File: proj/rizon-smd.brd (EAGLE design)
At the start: 49 parts, among them J1 PWRJACK5521, J2 DB9A-DS09AKG, P1 UART1(GND-TX-RX), P6 10k, U1 Z8400LQFP, U10 7432SOIC, U11 74138SOIC, U12 7400SOIC, U13 74590SOIC, U14 74590SOIC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

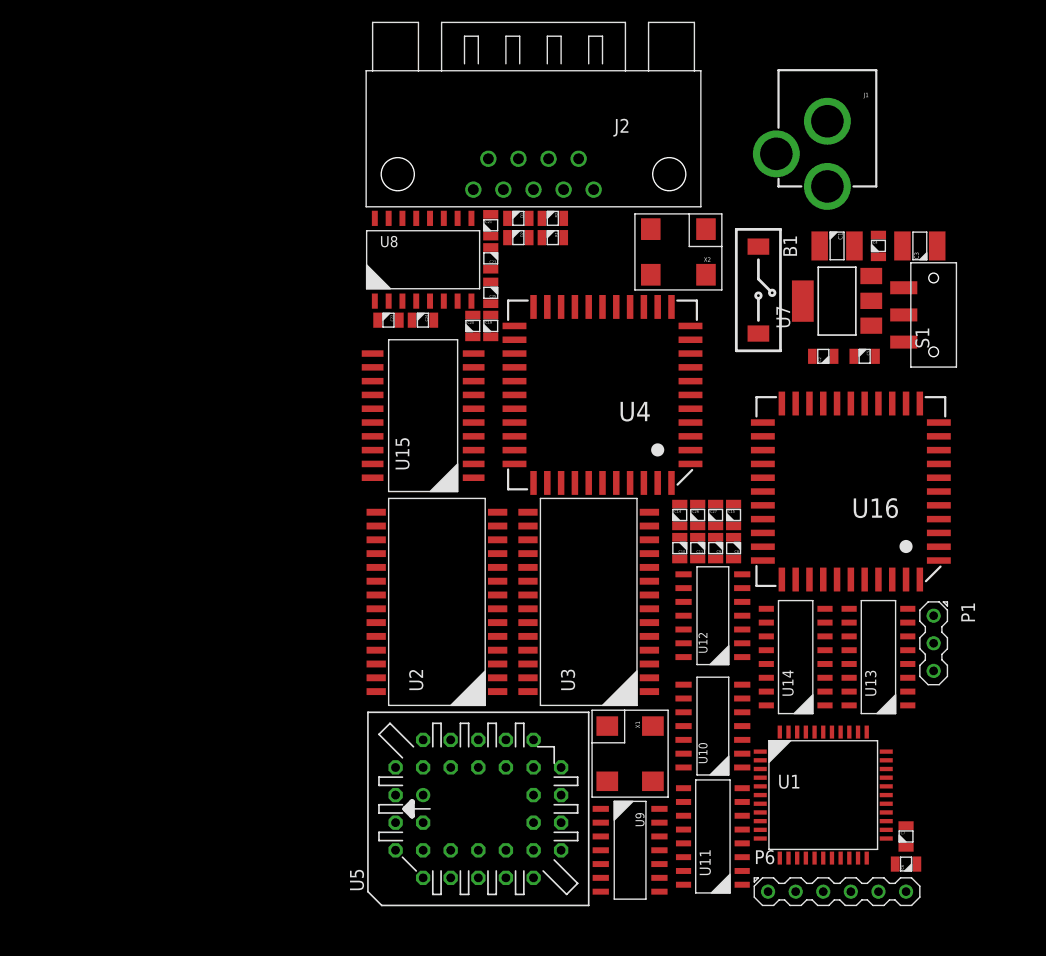
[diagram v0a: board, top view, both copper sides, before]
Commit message: Started routing SMD version of Rizon board
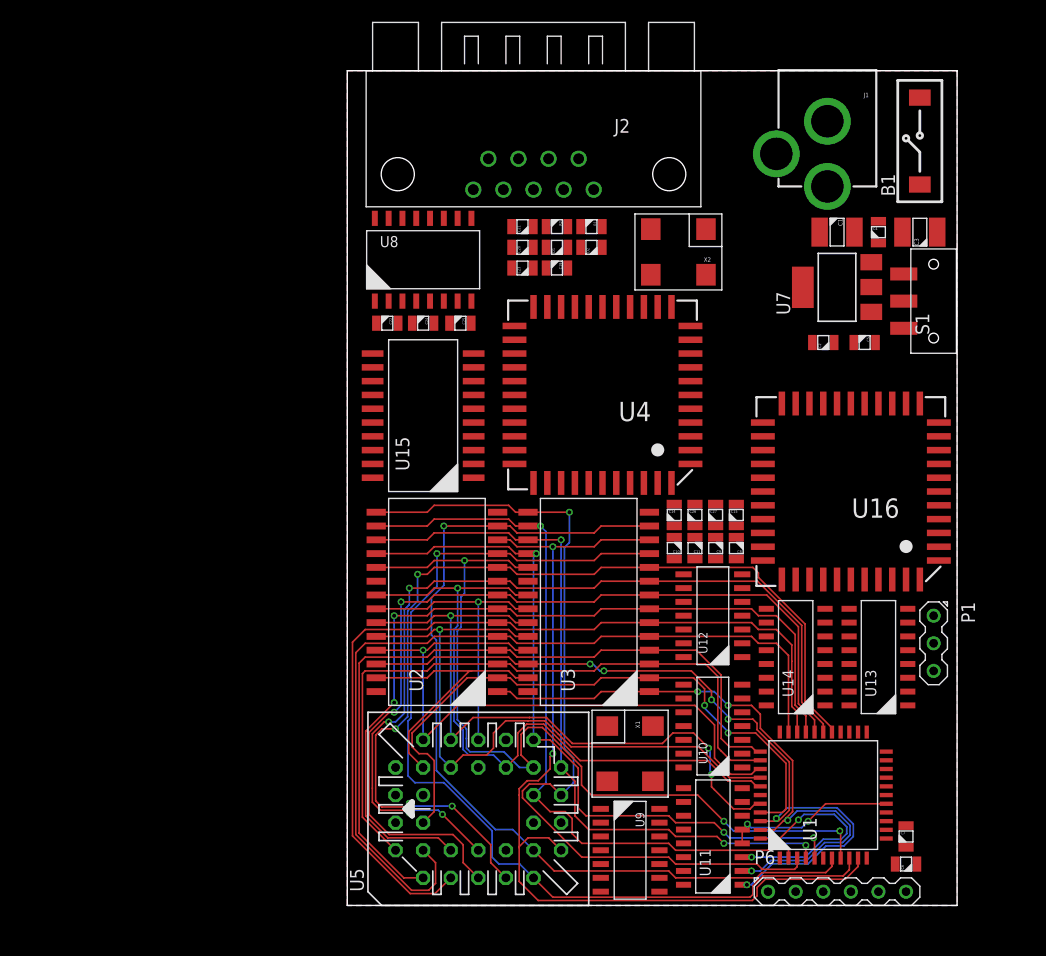
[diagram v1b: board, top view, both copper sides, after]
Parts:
- moved B1 20.2 mm to (81.3, 72.9), turned to 90 degrees
- moved C20 8.56 mm to (44.7, 63.1), turned to 0 degrees
- moved C19 8.10 mm to (47.9, 61.2), turned to 180 degrees
- moved D2 6.79 mm to (51.1, 63.1), turned to 0 degrees
- moved D1 4.44 mm to (47.9, 63.1), turned to 0 degrees
- moved C25 3.95 mm to (39.0, 56.1), turned to 180 degrees
- moved R1 3.70 mm to (51.1, 65.0)
- moved C23 3.05 mm to (44.7, 61.2), turned to 0 degrees
- moved C21 2.92 mm to (44.7, 65.0), turned to 0 degrees
- moved C1 1.27 mm to (73.7, 64.5)
- moved C2 1.27 mm to (72.4, 54.4)
- moved C3 1.27 mm to (81.3, 64.5)
- moved C4 1.27 mm to (77.5, 64.5)
- moved C5 1.27 mm to (76.2, 54.4)
- moved U7 1.27 mm to (73.7, 59.4)
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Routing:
- net DATA0: track 0.00 -> 90.9 mm, vias 0 -> 1
- net ADDR0: track 0.00 -> 89.2 mm, vias 0 -> 4
- net DATA1: track 0.00 -> 86.4 mm, vias 0 -> 2
- net DATA2: track 0.00 -> 84.3 mm, vias 0 -> 1
- net ADDR2: track 0.00 -> 83.4 mm, vias 0 -> 2
- net ADDR1: track 0.00 -> 82.8 mm, vias 0 -> 4
- net ADDR4: track 0.00 -> 80.5 mm
- net DATA7: track 0.00 -> 79.9 mm, vias 0 -> 3
- net DATA3: track 0.00 -> 79.1 mm, vias 0 -> 1
- net ADDR5: track 0.00 -> 78.7 mm
- net ADDR3: track 0.00 -> 76.7 mm, vias 0 -> 2
- net ADDR13: track 0.00 -> 72.5 mm, vias 0 -> 6
- net DATA4: track 0.00 -> 68.6 mm, vias 0 -> 1
- net ADDR6: track 0.00 -> 68.5 mm
- net DATA5: track 0.00 -> 67.0 mm, vias 0 -> 3
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- added copper zone on layer 1, net GND
- added copper zone on layer 16, net GND
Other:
- board outline added: 56.1 x 76.8 mm

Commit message: Added missing signal net (TIMER_OUT -> INT_TIMER) in Rizon I/O board Further routed SMD version of Rizon computer
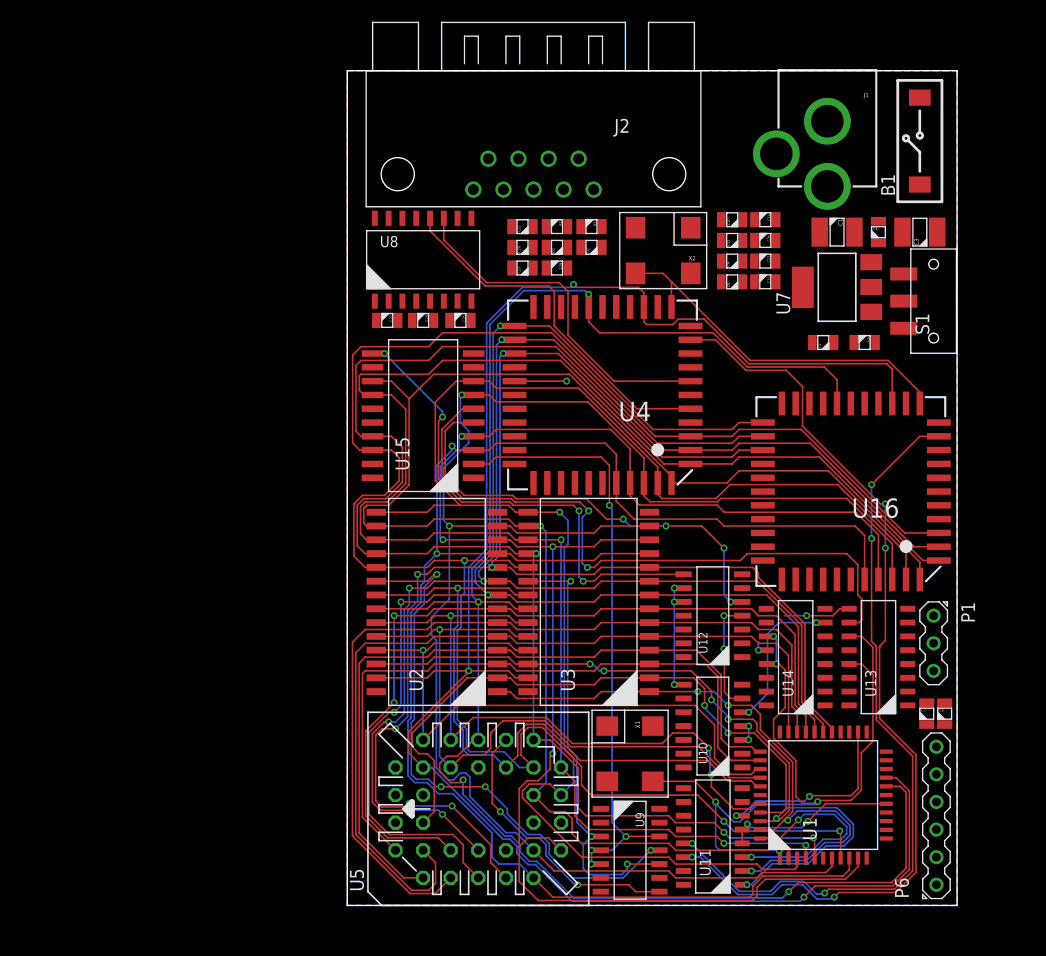
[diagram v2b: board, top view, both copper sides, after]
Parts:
- moved C10 30.7 mm to (64.0, 65.7), turned to 0 degrees
- moved C11 28.5 mm to (64.0, 63.8), turned to 0 degrees
- moved C14 28.4 mm to (67.1, 65.7), turned to 180 degrees
- moved C9 26.5 mm to (64.0, 61.8), turned to 0 degrees
- moved C26 26.1 mm to (67.1, 63.8), turned to 180 degrees
- moved C8 24.5 mm to (64.0, 59.9), turned to 0 degrees
- moved C27 23.8 mm to (67.1, 61.8), turned to 180 degrees
- moved C15 21.6 mm to (67.1, 59.9), turned to 180 degrees
- moved C6 14.3 mm to (83.6, 20.2), turned to 270 degrees
- moved P6 11.5 mm to (82.8, 10.8), turned to 90 degrees
- moved C7 11.5 mm to (81.9, 20.2)
- moved X2 1.40 mm to (57.7, 62.8)
- moved C22 0.25 mm to (32.3, 56.4)
- moved C24 0.25 mm to (35.6, 56.4)
- moved C25 0.25 mm to (39.0, 56.4)
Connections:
- removed net INT_TIMER: U10.P$5
- net TIMER_OUT: now also U10.P$5
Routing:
- net !WR: track 26.4 -> 167.4 mm, vias 0 -> 3
- net !RD: track 27.2 -> 158.5 mm, vias 1 -> 4
- net DATA7: track 79.9 -> 170.2 mm
- net DATA6: track 66.1 -> 153.6 mm
- net !IODEV1: track 0.00 -> 86.6 mm, vias 0 -> 4
- net DATA5: track 67.0 -> 151.5 mm
- net DATA4: track 68.6 -> 146.5 mm
- net CLK: track 0.00 -> 72.2 mm, vias 0 -> 5
- net !IODEV2: track 0.00 -> 69.8 mm, vias 0 -> 4
- net DATA2: track 84.3 -> 149.9 mm, vias 1 -> 2
- net DATA3: track 79.1 -> 144.6 mm
- net DATA1: track 86.4 -> 151.1 mm, vias 2 -> 4
- net !TIMER_CLR: track 0.00 -> 61.0 mm, vias 0 -> 2
- net DATA0: track 90.9 -> 149.7 mm, vias 1 -> 2
- net !ROM_EN: track 0.00 -> 57.6 mm, vias 0 -> 4
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
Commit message: Rizon SMD routing work
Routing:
- net !TIMER_CLR: track 61.0 -> 71.1 mm, vias 2 -> 4
- net N$3: track 7.69 -> 11.3 mm
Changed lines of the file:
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@@
 <wire x1="30.2768" y1="18.5928" x2="32.893" y2="21.209" width="0.1524" layer="1"/>
 <via x="32.893" y="21.209" extent="1-16" drill="0.35"/>
-<wire x1="32.893" y1="21.209" x2="32.893" y2="29.21" width="0.1524" layer="16"/>
 <via x="32.893" y="29.21" extent="1-16" drill="0.35"/>
 <wire x1="32.893" y1="29.21" x2="35.941" y2="29.21" width="0.1524" layer="1"/>
@@
 <wire x1="32.30805625" y1="8.763" x2="30.2768" y2="10.79425625" width="0.1524" layer="1"/>
 <wire x1="30.2768" y1="10.79425625" x2="30.2768" y2="18.5928" width="0.1524" layer="1"/>
+<wire x1="32.893" y1="21.209" x2="33.2232" y2="21.5392" width="0.1524" layer="16"/>
+<wire x1="33.2232" y1="28.8798" x2="32.893" y2="29.21" width="0.1524" layer="16"/>
+<wire x1="33.2232" y1="21.5392" x2="33.2232" y2="28.8798" width="0.1524" layer="16"/>
 </signal>
 <signal name="ADDR2">
@@
 <wire x1="65.405" y1="34.925" x2="74.549" y2="34.925" width="0.1524" layer="1"/>
 <wire x1="74.549" y1="34.925" x2="75.565" y2="33.909" width="0.1524" layer="1"/>
-<wire x1="75.565" y1="33.909" x2="75.565" y2="31.115" width="0.1524" layer="1"/>
+<wire x1="75.565" y1="31.115" x2="75.565" y2="33.909" width="0.1524" layer="1"/>
 <wire x1="75.565" y1="31.115" x2="75.946" y2="30.734" width="0.1524" layer="1"/>
 <wire x1="75.946" y1="30.734" x2="75.946" y2="28.829" width="0.1524" layer="1"/>
@@
 <wire x1="49.9872" y1="39.6748" x2="50.8" y2="38.862" width="0.1524" layer="1"/>
 <wire x1="43.9913125" y1="39.6748" x2="49.9872" y2="39.6748" width="0.1524" layer="1"/>
-<wire x1="64.77" y1="34.29" x2="67.15" y2="28.575" width="0" layer="19" extent="1-1"/>
+<wire x1="67.15" y1="28.575" x2="66.802" y2="28.575" width="0.1524" layer="1"/>
+<via x="66.802" y="28.575" extent="1-16" drill="0.35"/>
+<wire x1="66.802" y1="28.575" x2="67.43958125" y2="28.575" width="0.1524" layer="16"/>
+<wire x1="67.43958125" y1="28.575" x2="68.136790625" y2="29.272209375" width="0.1524" layer="16"/>
+<wire x1="68.136790625" y1="29.272209375" x2="68.70958125" y2="29.845" width="0.1524" layer="16"/>
+<wire x1="69.977" y1="29.845" x2="70.104" y2="29.972" width="0.1524" layer="16"/>
+<via x="70.104" y="29.972" extent="1-16" drill="0.35"/>
+<wire x1="70.104" y1="29.972" x2="70.612" y2="30.48" width="0.1524" layer="1"/>
+<wire x1="74.93" y1="30.48" x2="75.565" y2="31.115" width="0.1524" layer="1"/>
+<wire x1="68.70958125" y1="29.845" x2="69.977" y2="29.845" width="0.1524" layer="16"/>
+<wire x1="70.612" y1="30.48" x2="74.93" y2="30.48" width="0.1524" layer="1"/>
 </signal>
 <signal name="N$3">
@@
 <wire x1="67.15" y1="26.035" x2="66.421" y2="26.035" width="0.1524" layer="1"/>
 <via x="66.421" y="26.035" extent="1-16" drill="0.35"/>
-<wire x1="66.421" y1="26.035" x2="66.421" y2="26.797" width="0.1524" layer="16"/>
-<wire x1="68.834" y1="29.21" x2="70.866" y2="29.21" width="0.1524" layer="16"/>
 <via x="70.866" y="29.21" extent="1-16" drill="0.35"/>
 <wire x1="70.866" y1="29.21" x2="73.279" y2="29.21" width="0.1524" layer="1"/>
 <wire x1="73.279" y1="29.21" x2="73.914" y2="29.845" width="0.1524" layer="1"/>
 <wire x1="73.914" y1="29.845" x2="74.77" y2="29.845" width="0.1524" layer="1"/>
-<wire x1="66.421" y1="26.797" x2="68.834" y2="29.21" width="0" layer="19" extent="16-16"/>
+<wire x1="70.866" y1="29.21" x2="68.5056375" y2="29.21" width="0.1524" layer="16"/>
+<wire x1="68.5056375" y1="29.21" x2="66.421" y2="27.1253625" width="0.1524" layer="16"/>
+<wire x1="66.421" y1="27.1253625" x2="66.421" y2="26.035" width="0.1524" layer="16"/>
 </signal>
 <signal name="TIMER_OUT">

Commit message: Added breakouts to Rizon SMD
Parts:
- added P2: ADDR, dooba:PIN_16
- added P3: DATA, dooba:PIN_8
- added P4: CTL, dooba:PIN_16
- added P5: PWR, dooba:PIN_4
- moved C10 0.25 mm to (64.0, 65.4)
- moved C14 0.25 mm to (67.1, 65.4)
- moved C15 0.25 mm to (67.1, 59.7)
- moved C8 0.25 mm to (64.0, 59.7)
- moved C11 0.25 mm to (64.0, 63.5)
- moved C26 0.25 mm to (67.1, 63.5)
- moved C27 0.25 mm to (67.1, 61.6)
- moved C9 0.25 mm to (64.0, 61.6)
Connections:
- net !BUSACK: now also P4.7
- net !BUSREQ: now also P4.3, P6.4; no longer P6.3
- net !HALT: now also P4.10
- net !INT: now also P4.12, P6.1; no longer P6.2
- net !IORQ: now also P4.8
- net !M1: now also P4.1
- net !MREQ: now also P4.11
- net !NMI: now also P4.13, P6.2; no longer P6.1
- net !RD: now also P4.9
- net !RESET: now also P4.4, P6.5; no longer P6.4
- net !RFSH: now also P4.2
- net !ROM_EN: now also P4.14
- net !WAIT: now also P4.5, P6.3; no longer P6.5
- net !WR: now also P4.6
- net ADDR0: now also P2.1
- net ADDR1: now also P2.2
- net ADDR10: now also P2.11
- net ADDR11: now also P2.12
- net ADDR12: now also P2.13
- net ADDR13: now also P2.14
- net ADDR14: now also P2.15
- net ADDR15: now also P2.16
- net ADDR2: now also P2.3
- net ADDR3: now also P2.4
- net ADDR4: now also P2.5
- net ADDR5: now also P2.6
- net ADDR6: now also P2.7
- net ADDR7: now also P2.8
- net ADDR8: now also P2.9
- net ADDR9: now also P2.10
- net CLK: now also P4.15
- net DATA0: now also P3.1
- net DATA1: now also P3.2
- net DATA2: now also P3.3
- net DATA3: now also P3.4
- net DATA4: now also P3.5
- net DATA5: now also P3.6
- net DATA6: now also P3.7
- net DATA7: now also P3.8
- net GND: now also P4.16, P5.1, P5.3
- net VCC: now also P5.4
- net VIN: now also P5.2
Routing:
- net !RESET: track 0.00 -> 146.3 mm, vias 0 -> 9
- net VCC: track 0.00 -> 99.6 mm, vias 0 -> 2
- net !INT: track 0.00 -> 69.0 mm, vias 0 -> 5
- net RESET: track 0.00 -> 64.1 mm, vias 0 -> 5
- net INT_UART0: track 4.80 -> 52.8 mm, vias 1 -> 4
- net ADDR15: track 20.5 -> 67.0 mm, vias 2 -> 9
- net VIN: track 0.00 -> 37.8 mm, vias 0 -> 2
- net ADDR14: track 59.0 -> 89.4 mm, vias 4 -> 8
- net INT_UART1: track 0.00 -> 27.5 mm, vias 0 -> 2
- net ADDR10: track 63.1 -> 81.1 mm, vias 1 -> 3
- net !WR: track 167.4 -> 185.1 mm, vias 3 -> 5
- net ADDR11: track 61.7 -> 79.2 mm, vias 3 -> 5
- net CLK_UART0_RX: track 0.00 -> 17.3 mm, vias 0 -> 4
- net UART1_RX: track 0.00 -> 17.0 mm, vias 0 -> 2
- net !IODEV0: track 0.00 -> 16.8 mm, vias 0 -> 2
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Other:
- board size 56.1 x 76.8 mm -> 62.2 x 76.8 mm

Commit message: Rizon SMD routing
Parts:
- moved C7 1.70 mm to (83.4, 19.4), turned to 0 degrees
- moved P1 1.27 mm to (83.8, 26.7)
- moved C6 0.90 mm to (83.4, 21.1), turned to 0 degrees
- turned P5 to 270 degrees
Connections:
- net !BUSACK: now also P4.9; no longer P4.7
- net !BUSREQ: now also P4.10; no longer P4.3
- net !HALT: now also P4.5; no longer P4.10
- net !INT: now also P4.3; no longer P4.12
- net !IORQ: now also P4.7; no longer P4.8
- net !M1: now also P4.12; no longer P4.1
- net !MREQ: now also P4.6; no longer P4.11
- net !NMI: now also P4.4; no longer P4.13
- net !RD: now also P4.2; no longer P4.9
- net !RESET: now also P4.11; no longer P4.4
- net !RFSH: now also P4.13; no longer P4.2
- net !ROM_EN: now also P4.15; no longer P4.14
- net !WAIT: now also P4.8; no longer P4.5
- net !WR: now also P4.1; no longer P4.6
- net CLK: now also P4.14; no longer P4.15
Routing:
- net !ROM_EN: track 57.6 -> 104.2 mm, vias 4 -> 6
- net !RFSH: track 0.00 -> 24.1 mm, vias 0 -> 2
- net DATA0: track 149.0 -> 171.3 mm
- net !M1: track 18.0 -> 39.9 mm, vias 2 -> 4
- net DATA1: track 150.6 -> 171.4 mm, vias 4 -> 5
- net DATA2: track 149.9 -> 167.4 mm, vias 2 -> 3
- net CLK: track 72.2 -> 87.3 mm, vias 5 -> 7
- net !INT: track 69.0 -> 60.0 mm
- net UART1_RX: track 17.0 -> 8.94 mm, vias 2 -> 1
- net !IORQ: track 15.8 -> 22.3 mm, vias 2 -> 3
- net !MREQ: track 0.00 -> 6.11 mm, vias 0 -> 1
- net !HALT: track 0.00 -> 5.65 mm, vias 0 -> 1
- net UART1_TX: track 16.1 -> 11.2 mm, vias 2 -> 1
- net !RESET: track 146.3 -> 150.8 mm, vias 9 -> 10
- net !IODEV1: track 86.6 -> 87.5 mm

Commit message: Completed Rizon SMD board
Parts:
- moved B1 29.3 mm to (52.1, 70.4)
- moved J1 29.2 mm to (43.6, 73.5)
- moved P1 29.0 mm to (61.0, 44.5), flipped to the bottom
- moved C6 26.9 mm to (56.6, 23.4), turned to 90 degrees
- moved S1 26.2 mm to (59.7, 70.9)
- moved P5 25.9 mm to (61.0, 53.3), flipped to the bottom
- moved P3 25.5 mm to (1.27, 50.8), flipped to the bottom
- moved C5 25.5 mm to (50.8, 51.8)
- moved U16 25.5 mm to (49.5, 38.1)
- moved C20 25.5 mm to (19.3, 60.6)
- moved C21 25.5 mm to (19.3, 62.5)
- moved C22 25.5 mm to (6.86, 53.8)
- moved C23 25.5 mm to (19.3, 58.7)
- moved C24 25.5 mm to (10.2, 53.8)
- moved D2 25.5 mm to (25.7, 60.6)
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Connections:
- net !BUSREQ: now also P4.8; no longer P4.10
- net !HALT: now also P4.4; no longer P4.5
- net !INT: now also P4.1; no longer P4.3
- net !IORQ: now also P4.6; no longer P4.7
- net !MREQ: now also P4.5; no longer P4.6
- net !NMI: now also P4.2; no longer P4.4
- net !RD: now also P4.11; no longer P4.2
- net !RESET: now also P4.7; no longer P4.11
- net !WAIT: now also P4.3; no longer P4.8
- net !WR: now also P4.10; no longer P4.1
- net VIN: now also S1.1; no longer S1.3
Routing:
- net VCC: track 99.6 -> 436.0 mm, vias 2 -> 25
- net GND: track 0.00 -> 93.7 mm, vias 0 -> 442
- net !RD: track 158.5 -> 180.7 mm, vias 4 -> 6
- net !WR: track 185.1 -> 203.6 mm, vias 5 -> 7
- net VIN: track 37.8 -> 51.6 mm, vias 2 -> 4
- net !BUSACK: track 0.00 -> 13.7 mm, vias 0 -> 2
- net !BUSREQ: track 7.11 -> 18.6 mm, vias 1 -> 2
- net !IORQ: track 22.3 -> 28.4 mm
- net !RESET: track 150.8 -> 156.5 mm, vias 10 -> 11
- net !WAIT: track 8.74 -> 14.3 mm, vias 1 -> 2
- net !MREQ: track 6.11 -> 10.2 mm
- net UART1_TX: track 11.2 -> 7.22 mm, vias 1 -> 0
- net !INT: track 60.0 -> 63.8 mm
- net !NMI: track 5.68 -> 9.50 mm
- net !HALT: track 5.65 -> 8.65 mm
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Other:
- board text added: "!BUSACK"
- board text added: "!BUSREQ"
- board text added: "!HALT"
- board text added: "!INT"
- board text added: "!IORQ"
- board text added: "!M1"
- board text added: "!MREQ"
- board text added: "!NMI"
- board text added: "!RD"
- board text added: "!RESET"
- board text added: "!RFSH"
- board text added: "!ROM_EN"
- board text added: "!WAIT"
- board text added: "!WR"
- board text added: "100nF"
- board text added: "100uF"
- board text added: "10k"
- board text added: "10uF"
- board text added: "16550 UART"
- board text added: "18.432Mhz"
- board text added: "1k"
- board text added: "1uF"
- board text added: "4.0Mhz"
- board text added: "7400"
- board text added: "74138"
- board text added: "74273"
- board text added: "7432"
- board text added: "74590"
- board text added: "ADDR[0..15]"
- board text added: "AS6C62256 32kb SRAM"
- board text added: "AT28 C64B ROM"
- board text added: "CLK"
- board text added: "DATA[0..7]"
- board text added: "GND"
- board text added: "MAX232"
- board text added: "NCP1117 5.0V REG"
- board text added: "Power"
- board text added: "Reset"
- board text added: "Rizon"
- board text added: "Rizon Z80 Computer Z80 @ 4.0Mhz 64kb SRAM 8kb EEPROM 2 x UART Power: DC 6.5V 1A"
- board text added: "UART1_RX"
- board text added: "UART1_TX"
- board text added: "VCC"
- board text added: "VIN"
- board text added: "VIN: 6.5V"
- board text added: "Z80 CPU"
